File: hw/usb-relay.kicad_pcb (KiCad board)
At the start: 2 copper layers, 22 parts, among them IC1 ATTINY85-P, K1 RELAY_2RT, P1 USB_B, P2 CONN_02X03, Q1 BC548, U1 LM741

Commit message: Changes
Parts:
- added REF**: MountingHole_2-5mm, Mounting_Holes:MountingHole_2-5mm, F.Cu at (76.2, 92.7)
- added REF**: MountingHole_2-5mm, Mounting_Holes:MountingHole_2-5mm, F.Cu at (74.9, 137.2)
- moved R4 26.9 mm to (80.0, 96.5), turned to 0 degrees
- moved K1 21.1 mm to (71.1, 101.6), turned to 270 degrees
- moved F1 18.8 mm to (63.5, 114.3), turned to 270 degrees
- moved U1 18.0 mm to (91.4, 130.8), turned to 270 degrees
- moved P2 15.9 mm to (86.4, 108.0), turned to 180 degrees
- moved JP1 14.8 mm to (94.0, 121.9), turned to 0 degrees
- moved IC1 12.8 mm to (90.2, 120.7), turned to 180 degrees
- moved R2 12.5 mm to (80.0, 130.8), turned to 180 degrees
- moved D3 11.7 mm to (88.9, 109.2), turned to 90 degrees
- moved D2 10.9 mm to (82.5, 94.0), turned to 0 degrees
- moved R6 10.8 mm to (82.5, 128.3)
- moved D1 8.03 mm to (77.5, 97.8), turned to 180 degrees
- moved P_IN1 7.62 mm to (63.5, 94.0)
- moved Q1 5.39 mm to (69.8, 92.7), turned to 270 degrees
- moved P1 5.39 mm to (92.7, 101.6)
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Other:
- board outline added: 45.7 x 53.3 mm

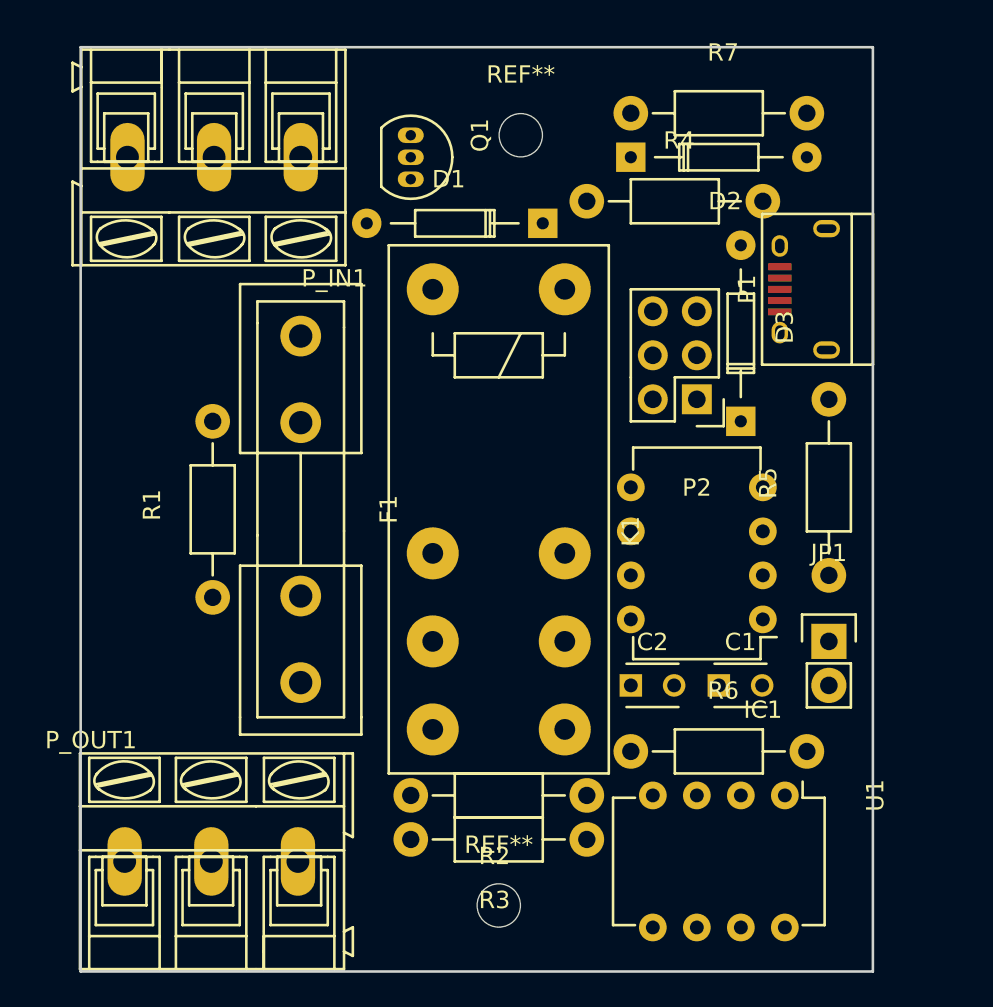
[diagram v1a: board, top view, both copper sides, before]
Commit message: Almost done, needs component values
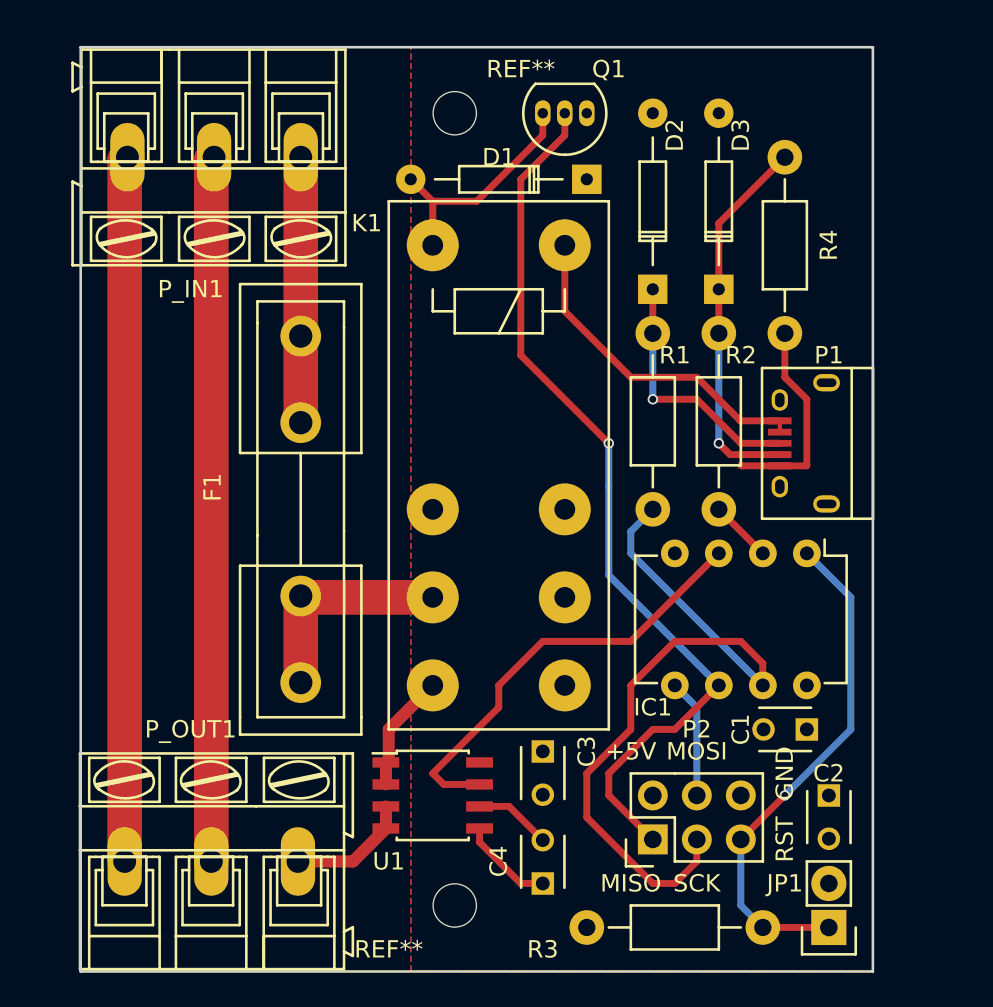
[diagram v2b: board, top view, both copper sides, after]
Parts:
- removed R5, R6, R7: R, Resistors_ThroughHole:Resistor_Horizontal_RM10mm
- removed the REF** at (76.2, 92.7)
- removed the REF** at (74.9, 137.2)
- added C3: C, Capacitors_ThroughHole:C_Disc_D3_P2.5, F.Cu at (77.5, 128.3)
- added C4: C, Capacitors_ThroughHole:C_Disc_D3_P2.5, F.Cu at (77.5, 135.9)
- added REF**: MountingHole_2-5mm, Mounting_Holes:MountingHole_2-5mm, F.Cu at (72.4, 91.4)
- added REF**: MountingHole_2-5mm, Mounting_Holes:MountingHole_2-5mm, F.Cu at (72.4, 137.2)
- U1: value LM741 -> ACS714; footprint Housings_DIP:DIP-8_W7.62mm -> Housings_SOIC:SOIC-8_3.9x4.9mm_Pitch1.27mm
- moved R1 25.9 mm to (83.8, 114.3)
- moved P2 25.5 mm to (83.8, 133.3), turned to 90 degrees
- moved U1 20.3 mm to (71.1, 130.8), turned to 0 degrees
- moved R2 18.2 mm to (87.6, 114.3), turned to 90 degrees
- moved JP1 16.5 mm to (94.0, 138.4), turned to 180 degrees
- moved R4 13.7 mm to (91.4, 104.1), turned to 90 degrees
- moved C2 13.1 mm to (94.0, 130.8), turned to 270 degrees
- moved R3 11.4 mm to (90.2, 138.4)
- moved Q1 10.2 mm to (80.0, 91.4), turned to 180 degrees
- moved P1 8.89 mm to (92.7, 110.5)
- moved D3 7.73 mm to (87.6, 101.6)
- moved D2 7.73 mm to (83.8, 101.6), turned to 90 degrees
- moved C1 5.68 mm to (92.7, 127.0), turned to 180 degrees
- moved IC1 4.58 mm to (92.7, 116.8), turned to 270 degrees
- moved D1 3.59 mm to (80.0, 95.2)
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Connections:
- net MISO renamed ICTL
- IC1 pad 3: Net-(IC1-Pad3) -> ADCIN
- K1 pad 12: Net-(K1-Pad12) -> (no net)
- K1 pad 14: Net-(K1-Pad14) -> (no net)
- K1 pad 16: Net-(K1-Pad16) -> (no net)
- K1 pad 3: Net-(K1-Pad3) -> (no net)
- P_OUT1 pad 2: Net-(P_OUT1-Pad2) -> Net-(P_IN1-Pad2)
- P_OUT1 pad 3: Net-(K1-Pad1) -> Net-(P_OUT1-Pad3)
- R1 pad 1: Net-(P_OUT1-Pad2) -> SCK
- R1 pad 2: Net-(P_IN1-Pad2) -> Net-(D2-Pad1)
- R2 pad 1: Net-(R2-Pad1) -> Net-(IC1-Pad2)
- R2 pad 2: Net-(P_IN1-Pad2) -> Net-(D3-Pad1)
- R3 pad 1: Net-(IC1-Pad3) -> RST
- R3 pad 2: Net-(R2-Pad1) -> +5V
- R4 pad 1: SCK -> +5V
- R4 pad 2: Net-(D2-Pad1) -> Net-(D3-Pad1)
- U1 pad 1: Net-(U1-Pad1) -> Net-(K1-Pad1)
- U1 pad 2: Net-(R2-Pad1) -> Net-(K1-Pad1)
- U1 pad 3: Net-(P_OUT1-Pad2) -> Net-(P_OUT1-Pad3)
- U1 pad 4: GND -> Net-(P_OUT1-Pad3)
- U1 pad 5: Net-(U1-Pad5) -> GND
- U1 pad 6: Net-(IC1-Pad3) -> Net-(C4-Pad2)
- U1 pad 7: +5V -> ADCIN
- U1 pad 8: (no net) -> +5V
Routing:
- net ICTL: track 0.00 -> 52.1 mm, vias 0 -> 1
- net SCK: track 0.00 -> 42.7 mm
- net Net-(P_IN1-Pad3): track 0.00 -> 40.7 mm
- net Net-(P_IN1-Pad2): track 0.00 -> 40.7 mm
- net RST: track 0.00 -> 29.6 mm, vias 0 -> 1
- net ADCIN: track 0.00 -> 25.5 mm
- net GND: track 0.00 -> 24.9 mm
- net Net-(D3-Pad1): track 0.00 -> 21.9 mm, vias 0 -> 1
- net Net-(F1-Pad1): track 0.00 -> 15.3 mm
- net Net-(D2-Pad1): track 0.00 -> 14.7 mm, vias 0 -> 1
- net Net-(D1-Pad2): track 0.00 -> 13.5 mm
- net Net-(F1-Pad2): track 0.00 -> 12.7 mm
- net +5V: track 0.00 -> 12.0 mm
- net Net-(P_OUT1-Pad3): track 0.00 -> 7.14 mm
- net MOSI: track 0.00 -> 6.88 mm
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- added copper zone on F.Cu, net +5V
- added copper zone on B.Cu, net GND
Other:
- net class Default: trace_width 0.25 -> 0.4
- net class less_power added: clearance 0.2, trace_width 0.7, via_dia 0.6, via_drill 0.4
- net class wall_power added: clearance 1, trace_width 2, via_dia 1, via_drill 0.8
- board text added: "+5V"
- board text added: "GND"
- board text added: "MISO"
- board text added: "MOSI"
- board text added: "RST"
- board text added: "SCK"

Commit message: Add a LED on MOSI pin, why not?
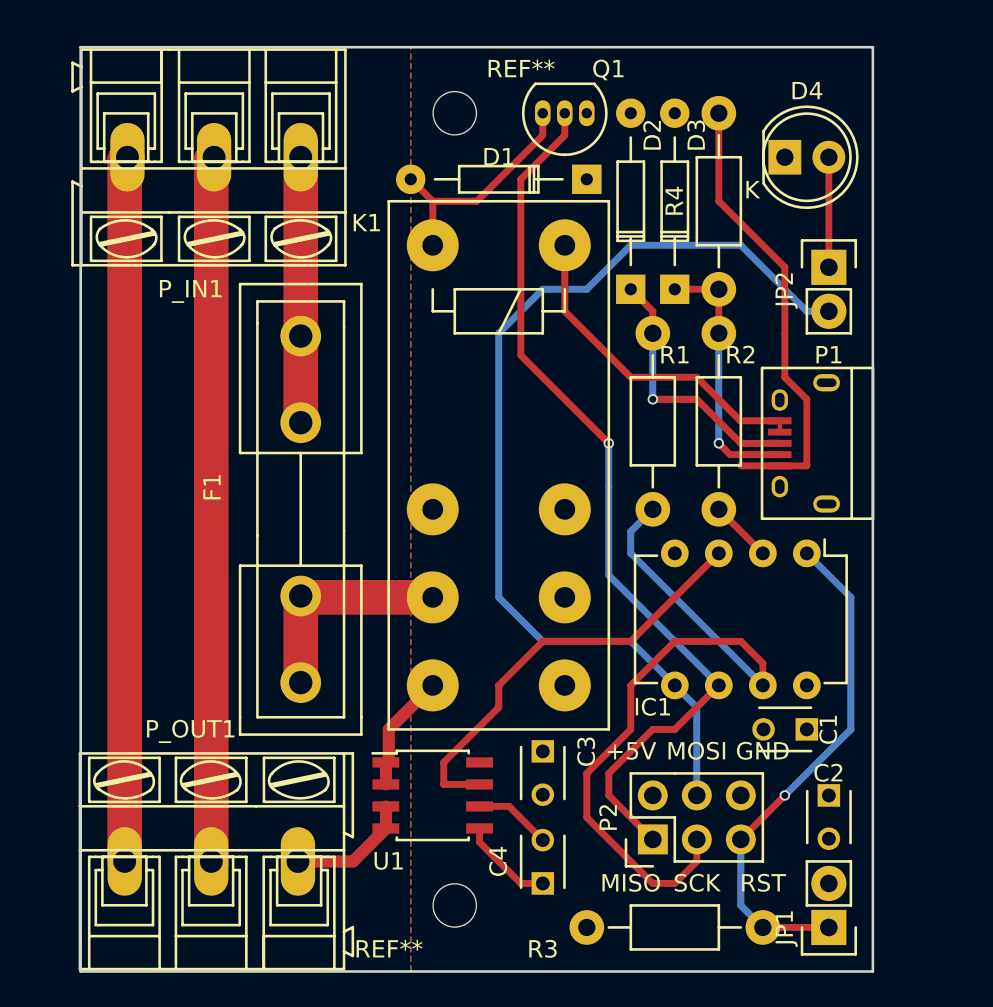
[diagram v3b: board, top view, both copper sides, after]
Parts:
- added D4: LED, LEDs:LED-5MM, F.Cu at (91.4, 94.0)
- added JP2: Jumper_NC_Small, Pin_Headers:Pin_Header_Straight_1x02, F.Cu at (94.0, 100.3)
- moved R4 13.3 mm to (87.6, 91.4), turned to 270 degrees
- moved D3 2.54 mm to (85.1, 101.6)
- moved D2 1.27 mm to (82.5, 101.6)
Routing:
- net MOSI: track 6.88 -> 57.1 mm
- net +5V: track 12.0 -> 26.3 mm
- net Net-(D3-Pad1): track 21.9 -> 15.2 mm
- net Net-(D4-Pad2): track 0.00 -> 6.35 mm
- net Net-(D2-Pad1): track 14.7 -> 15.3 mm
- net ADCIN: track 25.5 -> 25.0 mm

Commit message: Remove the reset jumper
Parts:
- removed JP1: Jumper_NO_Small, Pin_Headers:Pin_Header_Straight_1x02
- moved C2 4.02 mm to (92.7, 127.0)
- moved C1 2.54 mm to (90.2, 127.0)
- moved R3 1.27 mm to (91.4, 138.4)
- renumbered REF** to H0, REF** to H1
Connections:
- net RST renamed Net-(IC1-Pad1)
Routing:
- net Net-(IC1-Pad1): track 29.6 -> 30.4 mm, vias 1 -> 0

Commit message: A change?
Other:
- board text added: "Copyright 2016 Joakim Jalap"
- board text added: "USB relay v 0.1"
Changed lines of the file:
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@@
     (area 50.724999 87.554999 96.595001 141.045001)
     (thickness 1.6)
-    (drawings 10)
+    (drawings 12)
     (tracks 115)
     (zones 0)
@@
     (descr "Diode, DO-35,  SOD27, Horizontal, RM 10mm")
     (tags "Diode, DO-35, SOD27, Horizontal, RM 10mm, 1N4148,")
-    (fp_text reference D2 (at 8.89 1.27 90) (layer F.SilkS)
+    (fp_text reference D2 (at 12.7 0 90) (layer F.SilkS)
       (effects (font (size 1 1) (thickness 0.15)))
     )
@@
     (descr "Diode, DO-35,  SOD27, Horizontal, RM 10mm")
     (tags "Diode, DO-35, SOD27, Horizontal, RM 10mm, 1N4148,")
-    (fp_text reference D3 (at 8.89 1.27 90) (layer F.SilkS)
+    (fp_text reference D3 (at 12.7 0 90) (layer F.SilkS)
       (effects (font (size 1 1) (thickness 0.15)))
     )
@@
     (descr "Fuseholder, 5x20, open, horizontal, Type-I, Inline,")
     (tags "Fuseholder, 5x20, open, horizontal, Type-I, Inline, Sicherungshalter, offen,")
-    (fp_text reference F1 (at -1.27 5.08 270) (layer F.SilkS)
+    (fp_text reference F1 (at 0 3.81 270) (layer F.SilkS)
       (effects (font (size 1 1) (thickness 0.15)))
     )
@@
     (descr "Resistor, Axial,  RM 10mm, 1/3W")
     (tags "Resistor Axial RM 10mm 1/3W")
-    (fp_text reference R4 (at -1.27 -1.905 270) (layer F.SilkS)
+    (fp_text reference R4 (at -2.54 0 270) (layer F.SilkS)
       (effects (font (size 1 1) (thickness 0.15)))
     )
@@
     (descr "Capacitor 3mm Disc, Pitch 2.5mm")
     (tags Capacitor)
-    (fp_text reference C1 (at -1.27 0 450) (layer F.SilkS)
+    (fp_text reference C1 (at 4.445 0.635 180) (layer F.SilkS)
       (effects (font (size 1 1) (thickness 0.15)))
     )
@@
     (descr "Capacitor 3mm Disc, Pitch 2.5mm")
     (tags Capacitor)
-    (fp_text reference C2 (at -1.27 0 360) (layer F.SilkS)
+    (fp_text reference C2 (at 1.27 -2.54 450) (layer F.SilkS)
       (effects (font (size 1 1) (thickness 0.15)))
     )
@@
     (descr "8-lead dip package, row spacing 7.62 mm (300 mils)")
     (tags "dil dip 2.54 300")
-    (fp_text reference IC1 (at 8.89 8.89 360) (layer F.SilkS)
+    (fp_text reference IC1 (at 3.81 10.795 450) (layer F.SilkS)
       (effects (font (size 1 1) (thickness 0.15)))
     )
@@
     (descr "TO-92 leads in-line, narrow, oval pads, drill 0.6mm (see NXP sot054_po.pdf)")
     (tags "to-92 sc-43 sc-43a sot54 PA33 transistor")
-    (fp_text reference Q1 (at -1.27 2.54 180) (layer F.SilkS)
+    (fp_text reference Q1 (at 1.27 2.54 180) (layer F.SilkS)
       (effects (font (size 1 1) (thickness 0.15)))
     )
@@
     (descr "Relay, DPST, Schrack-RT2, RM5mm,")
     (tags "Relay, DPST,  Schrack-RT1, RM5mm, Reais, 2 x um,")
-    (fp_text reference K1 (at -1.27 3.81 360) (layer F.SilkS)
+    (fp_text reference K1 (at 15.24 3.175 450) (layer F.SilkS)
       (effects (font (size 1 1) (thickness 0.15)))
     )
@@
     (descr "Resistor, Axial,  RM 10mm, 1/3W")
     (tags "Resistor Axial RM 10mm 1/3W")
-    (fp_text reference R3 (at 12.7 -1.27 180) (layer F.SilkS)
+    (fp_text reference R3 (at -2.54 -0.635 180) (layer F.SilkS)
       (effects (font (size 1 1) (thickness 0.15)))
     )
@@
     (descr "Mounting hole, Befestigungsbohrung, 2,5mm, No Annular, Kein Restring,")
     (tags "Mounting hole, Befestigungsbohrung, 2,5mm, No Annular, Kein Restring,")
-    (fp_text reference H1 (at -3.81 0) (layer F.SilkS)
+    (fp_text reference H1 (at -3.175 -2.54) (layer F.SilkS)
       (effects (font (size 1 1) (thickness 0.15)))
     )
@@
     (descr "Mounting hole, Befestigungsbohrung, 2,5mm, No Annular, Kein Restring,")
     (tags "Mounting hole, Befestigungsbohrung, 2,5mm, No Annular, Kein Restring,")
-    (fp_text reference H0 (at -3.81 2.54) (layer F.SilkS)
+    (fp_text reference H0 (at 3.175 2.54) (layer F.SilkS)
       (effects (font (size 1 1) (thickness 0.15)))
     )
@@
       (rotate (xyz 0 0 90))
     )
+  )
+  (gr_text "USB relay\nv 0.1" (at 55.245 109.855 270) (layer F.SilkS)
+    (effects (font (size 1.5 1.5) (thickness 0.3)))
+  )
+  (gr_text "Copyright 2016\nJoakim Jalap" (at 52.705 121.285 270) (layer F.SilkS)
+    (effects (font (size 1 1) (thickness 0.15)))
   )
   (gr_text RST (at 90.17 135.89) (layer F.SilkS)
@@
   (segment (start 68.42 132.715) (end 68.42 131.445) (width 0.7) (layer F.Cu) (net 17))
   (segment (start 93.98 100.33) (end 93.98 93.98) (width 0.4) (layer F.Cu) (net 18))
-  (segment (start 88.9 133.35) (end 88.9 135.89) (width 0.4) (layer F.Cu) (net 19) (status 400000))
-  (segment (start 88.9 135.89) (end 91.44 138.43) (width 0.4) (layer F.Cu) (net 19) (status 800000))
+  (segment (start 88.9 133.35) (end 88.9 135.89) (width 0.4) (layer F.Cu) (net 19))
+  (segment (start 88.9 135.89) (end 91.44 138.43) (width 0.4) (layer F.Cu) (net 19))
   (segment (start 95.25 133.35) (end 95.25 134.62) (width 0.4) (layer B.Cu) (net 19))
   (segment (start 95.25 127) (end 95.25 119.38) (width 0.4) (layer B.Cu) (net 19))
   (segment (start 92.71 116.84) (end 95.25 119.38) (width 0.4) (layer B.Cu) (net 19))
   (segment (start 95.25 127) (end 95.25 133.35) (width 0.4) (layer B.Cu) (net 19))
-  (segment (start 95.25 134.62) (end 91.44 138.43) (width 0.4) (layer B.Cu) (net 19) (status 800000))
+  (segment (start 95.25 134.62) (end 91.44 138.43) (width 0.4) (layer B.Cu) (net 19))
   (zone (net 1) (net_name +5V) (layer F.Cu) (hatch edge 0.508)
     (connect_pads (clearance 0.508))
